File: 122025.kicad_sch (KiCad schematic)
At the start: 49 parts, among them J1 IN, J2 OUT, J3 PWR, J4 LED, J5 GND, Q1 2N5088, Q2 2N4401, U1 JRC4558

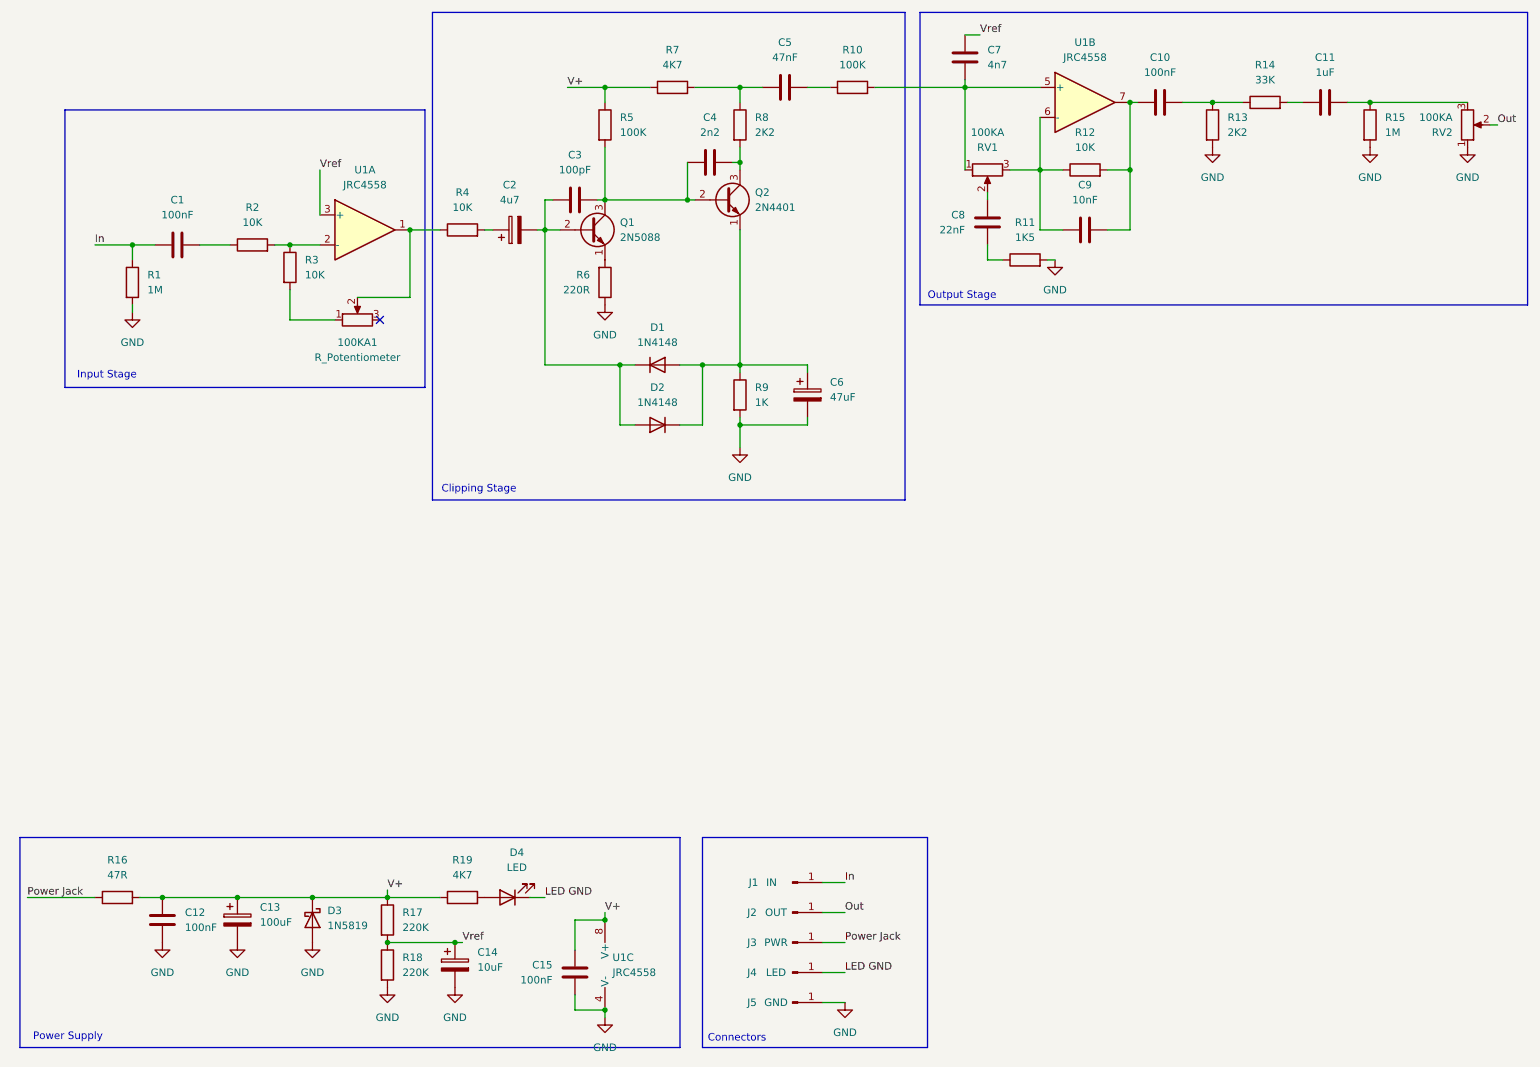
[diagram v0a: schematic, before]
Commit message: Minor value and reference fix
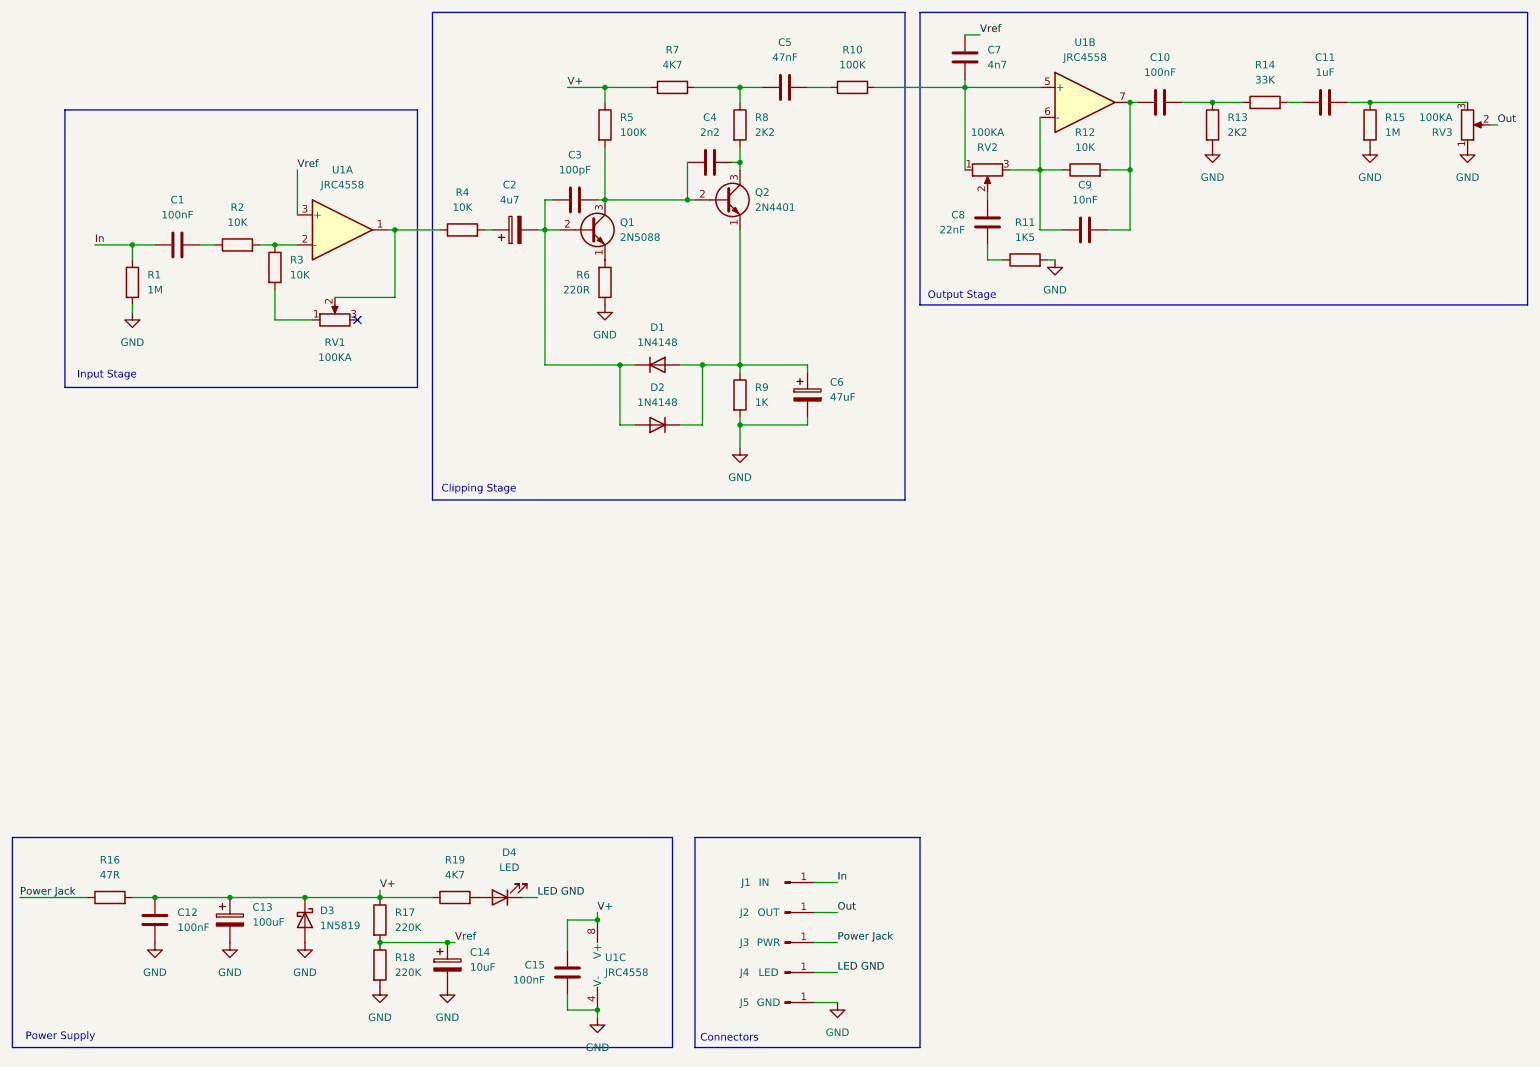
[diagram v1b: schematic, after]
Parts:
- RV1: renamed from 100KA1; value R_Potentiometer -> 100KA
- renumbered RV1 to RV2, RV2 to RV3
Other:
- moved on the sheet: C12, C13, C14, C15, D3, D4, J1, J2, J3, J4, J5, R16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

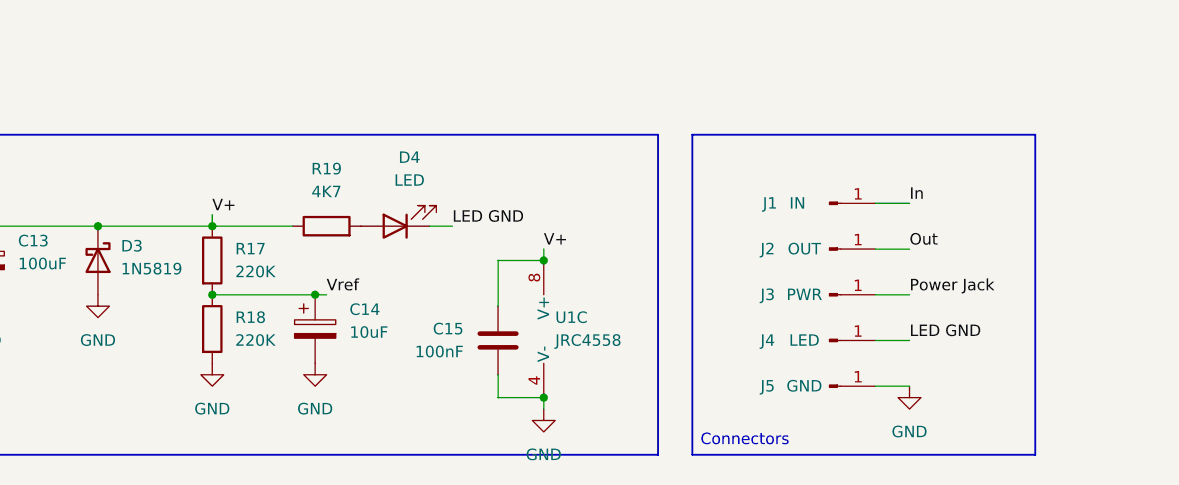
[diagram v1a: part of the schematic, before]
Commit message: Added footprints, solved ERC, and created BOM
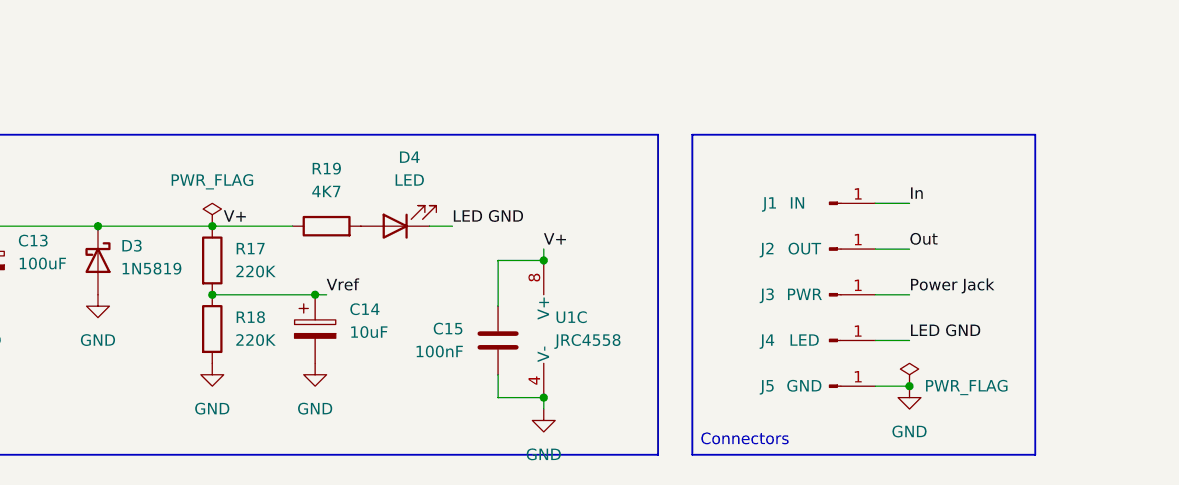
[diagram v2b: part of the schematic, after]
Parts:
- C1, C10, C11, C12, C15, C4, C5, C7, C8, C9: footprint (none) -> Capacitor_THT:C_Rect_L7.0mm_W2.5mm_P5.00mm
- C13: footprint (none) -> Capacitor_THT:CP_Radial_D6.3mm_P2.50mm
- C14, C2, C6: footprint (none) -> Capacitor_THT:CP_Radial_D5.0mm_P2.50mm
- C3: footprint (none) -> Capacitor_THT:C_Disc_D5.0mm_W2.5mm_P5.00mm
- R1, R10, R11, R12, R13, R14, R15, R17, R18, R2, R3, R4, R5, R6, R7, R8, R9: footprint (none) -> Resistor_THT:R_Axial_DIN0207_L6.3mm_D2.5mm_P7.62mm_Horizontal
- R16, R19: footprint (none) -> Resistor_THT:R_Axial_DIN0309_L9.0mm_D3.2mm_P12.70mm_Horizontal
- RV1, RV2, RV3: footprint (none) -> Potentiometer_THT:Potentiometer_Alpha_RD901F-40-00D_Single_Vertical
- U1: footprint (none) -> Package_DIP:DIP-8_W7.62mm_Socket
